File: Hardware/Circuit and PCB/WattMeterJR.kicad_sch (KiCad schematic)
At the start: 56 parts, among them IC1 ATM90E32AS-AU-R, J1 502570-0893, J2 L In, J3 N, J4 L Out, J5 Input, J6 Debug, J7 PWR/GND, P1 Nema 5-15-P, P2 Nema 5-15-R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

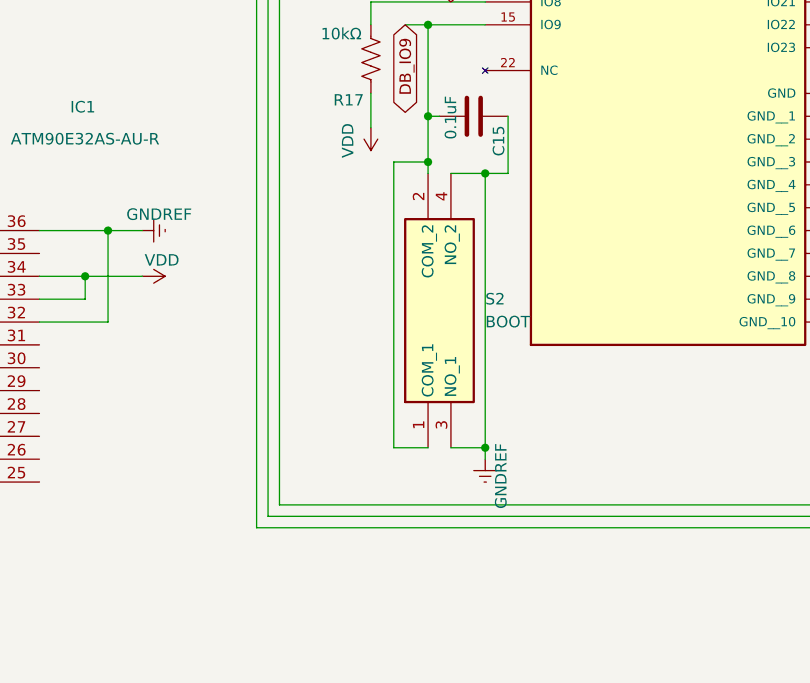
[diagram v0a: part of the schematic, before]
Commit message: Add pullup for GPIO9
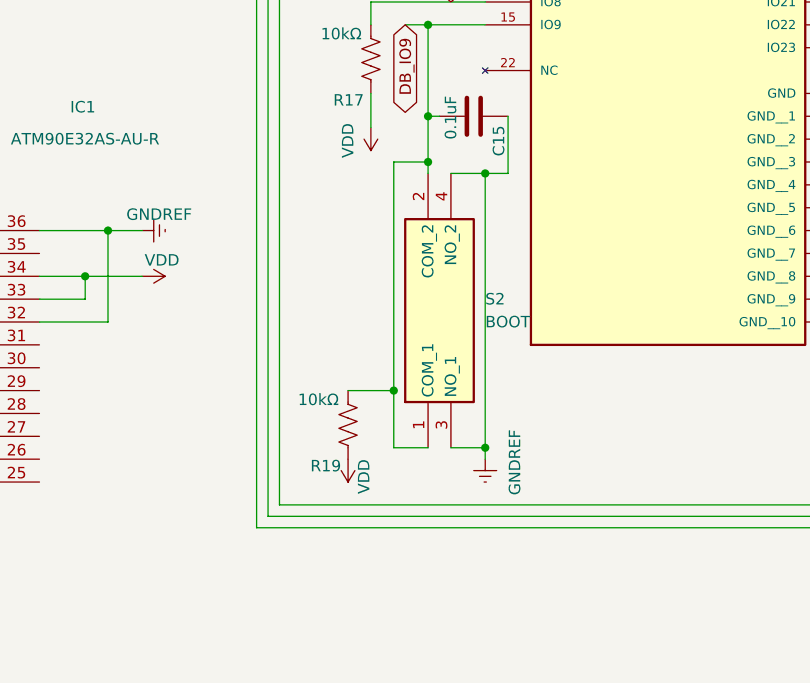
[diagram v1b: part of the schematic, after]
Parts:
- added R19: 10kΩ, Resistor_SMD:R_0805_2012Metric_Pad1.20x1.40mm_HandSolder, symbol Device:R_US
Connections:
- net DB_IO9: now also R19.1
- net VDD: now also R19.2
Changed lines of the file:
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@@
 	)
 	(junction
+		(at 167.64 140.97)
+		(diameter 0)
+		(color 0 0 0 0)
+	)
+	(junction
 		(at 85.09 114.3)
 		(diameter 0)
@@
 	(wire
 		(pts
-			(xy 167.64 147.32) (xy 167.64 115.57)
+			(xy 167.64 147.32) (xy 167.64 140.97)
 		)
 		(stroke
@@
 	(wire
 		(pts
+			(xy 167.64 140.97) (xy 167.64 115.57)
+		)
+		(stroke
+			(width 0)
+			(type default)
+		)
+	)
+	(wire
+		(pts
 			(xy 232.41 156.21) (xy 232.41 86.36)
 		)
@@
 	(wire
 		(pts
+			(xy 162.56 140.97) (xy 167.64 140.97)
+		)
+		(stroke
+			(width 0)
+			(type default)
+		)
+	)
+	(wire
+		(pts
 			(xy 114.3 81.28) (xy 120.65 81.28)
 		)
@@
 		)
 		(property "Value" "GNDREF"
-			(at 179.578 146.812 90)
+			(at 181.102 145.288 90)
 			(effects
 				(font
@@
 	)
 	(symbol
+		(lib_id "Device:R_US")
+		(at 162.56 144.78 0)
+		(unit 1)
+		(exclude_from_sim no)
+		(in_bom yes)
+		(on_board yes)
+		(dnp no)
+		(property "Reference" "R19"
+			(at 161.798 149.352 0)
+			(effects
+				(font
+					(size 1.27 1.27)
+				)
+				(justify right)
+			)
+		)
+		(property "Value" "10kΩ"
+			(at 161.544 141.986 0)
+			(effects
+				(font
+					(size 1.27 1.27)
+				)
+				(justify right)
+			)
+		)
+		(property "Footprint" "Resistor_SMD:R_0805_2012Metric_Pad1.20x1.40mm_HandSolder"
+			(at 163.576 145.034 90)
+			(effects
+				(font
+					(size 1.27 1.27)
+				)
+				(hide yes)
+			)
+		)
+		(property "Datasheet" "~"
+			(at 162.56 144.78 0)
+			(effects
+				(font
+					(size 1.27 1.27)
+				)
+				(hide yes)
+			)
+		)
+		(property "Description" "Resistor, US symbol"
+			(at 162.56 144.78 0)
+			(effects
+				(font
+					(size 1.27 1.27)
+				)
+				(hide yes)
+			)
+		)
+		(pin "1"
+		)
+		(pin "2"
+		)
+		(instances
+			(project "WattMeterJR"
+				(path "/a630c2f5-1474-4f68-8bdc-13f8f5fb42d0"
+					(reference "R19")
+					(unit 1)
+				)
+			)
+		)
+	)
+	(symbol
 		(lib_id "Device:LED")
 		(at 173.99 35.56 180)
@@
 					(unit 1)
 				)
+			)
+		)
+	)
+	(symbol
+		(lib_id "power:VDD")
+		(at 162.56 148.59 180)
+		(unit 1)
+		(exclude_from_sim no)
+		(in_bom yes)
+		(on_board yes)
+		(dnp no)
+		(property "Reference" "#PWR020"
+			(at 162.56 144.78 0)
+			(effects
+				(font
+					(size 1.27 1.27)
+				)
+				(hide yes)
+			)
+		)
+		(property "Value" "VDD"
+			(at 164.338 148.59 90)
+			(effects
+				(font
+					(size 1.27 1.27)
+				)
+				(justify left)
+			)
+		)
+		(property "Footprint" ""
+			(at 162.56 148.59 0)
+			(effects
+				(font
+					(size 1.27 1.27)
+				)
+				(hide yes)
+			)
+		)
+		(property "Datasheet" ""
+			(at 162.56 148.59 0)
+			(effects
+				(font
+					(size 1.27 1.27)
+				)
+				(hide yes)
+			)
+		)
+		(property "Description" "Power symbol creates a global label with name \"VDD\""
+			(at 162.56 148.59 0)
+			(effects
+				(font
+					(size 1.27 1.27)
+				)
+				(hide yes)
+			)
+		)
+		(pin "1"
+		)
+		(instances
+			(project "WattMeterJR"
+				(path "/a630c2f5-1474-4f68-8bdc-13f8f5fb42d0"
+					(reference "#PWR020")
+					(unit 1)
+				)
